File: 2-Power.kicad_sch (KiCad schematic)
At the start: 17 parts, among them J201 DC IN 5.5/2.1mm, J202 9V Battery Connector, U201 ZXMP3A17E6TA

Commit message: Schematic: adding 9V battery clip
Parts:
- J202: LCSC Part # (none) -> -; Mfr (none) -> Keystone; Mfr Part # (none) -> 232; Mouser Part # (none) -> 534-232; Purpose (none) -> connecting the battery to DC IN jack lugs; Source (none) -> Mouser; TME Part # (none) -> KEYS232; now in the parts list
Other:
- note added: "alt: 232-M, 233, 234"
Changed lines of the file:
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@@
+		)
+	)
+	(text "alt: 232-M, 233, 234"
+		(exclude_from_sim no)
+		(at 48.26 83.82 0)
+		(effects
+			(font
+				(size 1 1)
+			)
+			(justify left bottom)
 		)
 	)
@@
 	(text "connected directly to\nDC IN jack lugs"
 		(exclude_from_sim no)
-		(at 48.26 82.55 0)
+		(at 48.26 80.01 0)
 		(effects
 			(font
@@
 		(unit 1)
 		(exclude_from_sim no)
-		(in_bom no)
+		(in_bom yes)
 		(on_board no)
 		(dnp no)
@@
 			)
 		)
-		(property "Datasheet" ""
+		(property "Datasheet" "https://cz.mouser.com/datasheet/2/215/232_234-741236.pdf"
 			(at 39.37 74.295 0)
 			(effects
@@
 			)
 		)
-		(property "Purpose" ""
+		(property "Purpose" "connecting the battery to DC IN jack lugs"
 			(at 39.37 77.47 0)
 			(effects
@@
 					(size 1.27 1.27)
 				)
-			)
-		)
+				(hide yes)
+			)
+		)
+		(property "LCSC Part #" "-"
+			(at 39.37 77.47 0)
+			(effects
+				(font
+					(size 1.27 1.27)
+				)
+				(hide yes)
+			)
+		)
+		(property "Mfr" "Keystone"
+			(at 39.37 77.47 0)
+			(effects
+				(font
+					(size 1.27 1.27)
+				)
+				(hide yes)
+			)
+		)
+		(property "Mfr Part #" "232"
+			(at 39.37 77.47 0)
+			(effects
+				(font
+					(size 1.27 1.27)
+				)
+				(hide yes)
+			)
+		)
+		(property "Mouser Part #" "534-232 "
+			(at 39.37 77.47 0)
+			(effects
+				(font
+					(size 1.27 1.27)
+				)
+				(hide yes)
+			)
+		)
+		(property "Source" "Mouser"
+			(at 39.37 77.47 0)
+			(effects
+				(font
+					(size 1.27 1.27)
+				)
+				(hide yes)
+			)
+		)
+		(property "TME Part #" "KEYS232"
+			(at 39.37 77.47 0)
+			(effects
+				(font
+					(size 1.27 1.27)
+				)
+				(hide yes)
+			)
+		)

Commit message: Schematics: improving Purpose of some components
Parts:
- S201: Purpose ON/OFF switch for DC + true bypass switch for audio -> 4PDT. ON/OFF switch for DC + true bypass switch for audio; Source TME -> Mouser
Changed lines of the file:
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@@
 			)
 		)
-		(property "Purpose" "ON/OFF switch for DC + true bypass switch for audio"
+		(property "Purpose" "4PDT. ON/OFF switch for DC + true bypass switch for audio"
 			(at 49.53 121.92 0)
 			(effects
@@
 			)
 		)
-		(property "Source" "TME"
+		(property "Source" "Mouser"
 			(at 49.53 121.92 0)
 			(effects

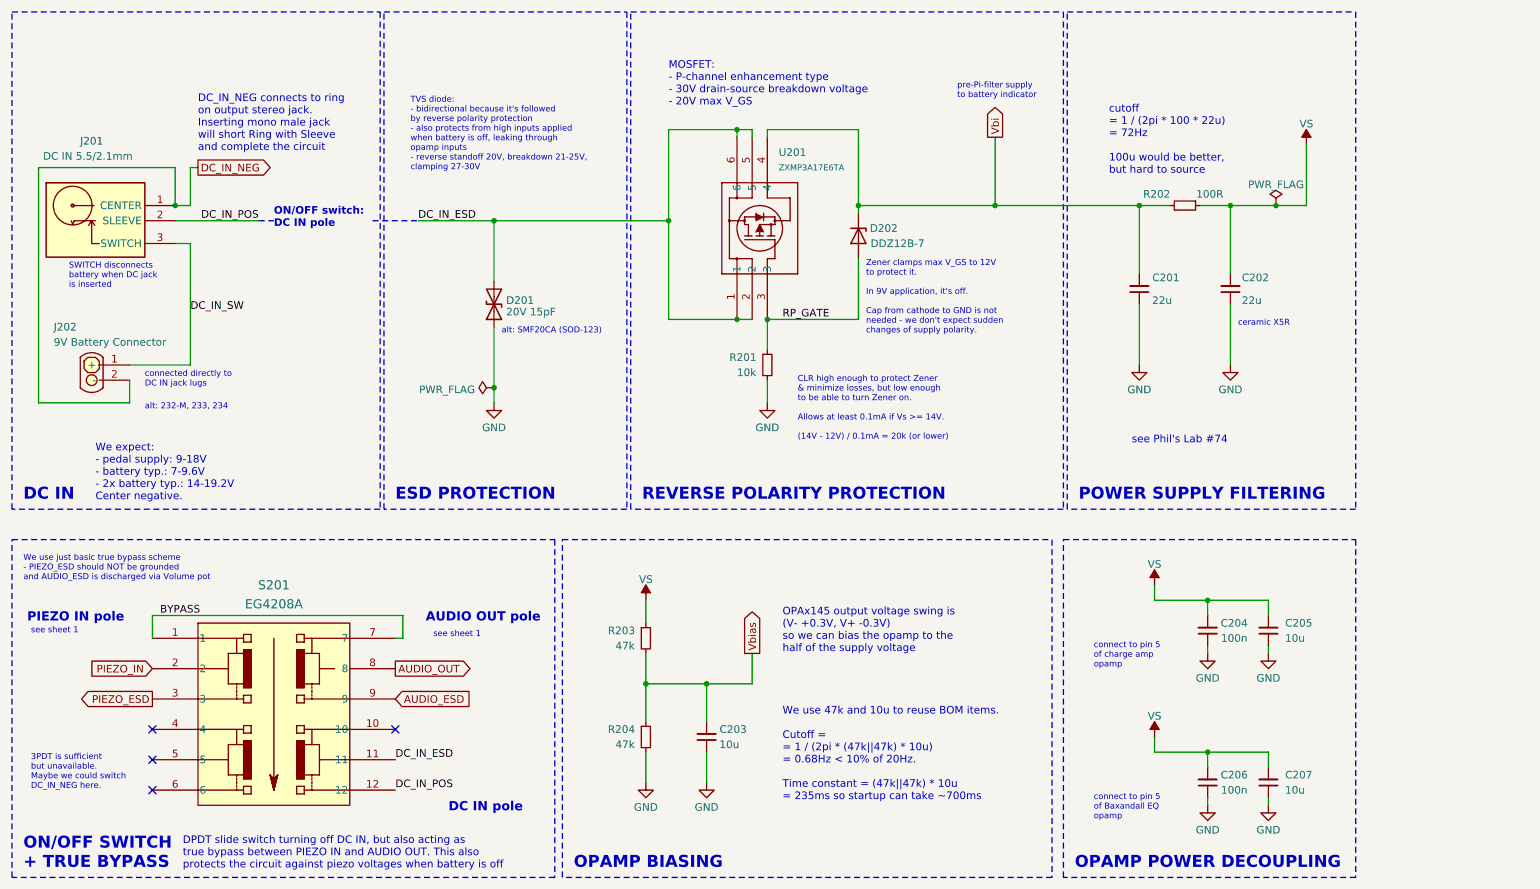
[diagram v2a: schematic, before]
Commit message: Schematic, PCB: moving DC ESD protection in front of the switch. Using one 22uF bulk decoupling cap where DC enters the board instead of two 10uF near opamps. Using 22uF instead of 10uF in opamp biasing to remove 10uF from BOM completely
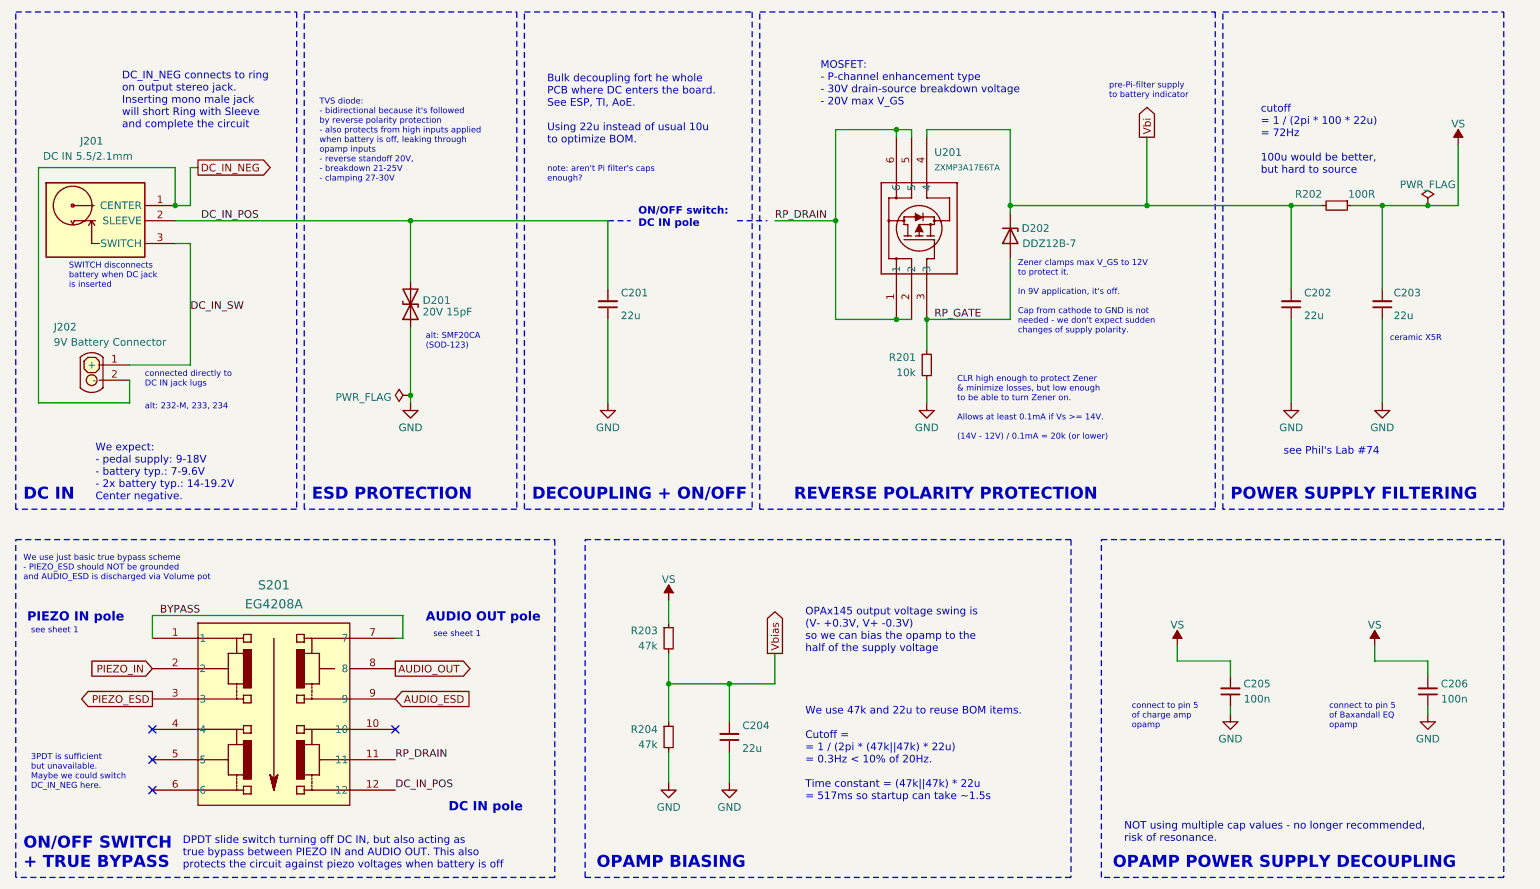
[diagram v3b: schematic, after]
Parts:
- removed C203, C205, C207: 10u, library:cap_CL21A106KAYNNNE, symbol Device:C_Small
- added C201, C204: 22u, library:cap_CL31A226KAHNNNE, symbol Device:C_Small
- renumbered C201 to C202, C202 to C203, C204 to C205
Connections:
- net DC_IN_POS: now also D201.2 (A2), C201.2
- net GND: now also C201.1, C204.1
- net Vbias: now also C204.2
- net DC_IN_ESD renamed RP_DRAIN
- net RP_DRAIN: no longer D201.2 (A2)
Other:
- note added: "Bulk decoupling fort he whole PCB where DC enters the board. See ESP, TI, AoE. Using 22u instead of usual 10u to optimize BOM."
- note added: "DECOUPLING + ON/OFF"
- note added: "NOT using multiple cap values - no longer recommended, risk of resonance."
- note added: "OPAMP POWER SUPPLY DECOUPLING"
- note added: "TVS diode: - bidirectional because it's followed by reverse polarity protection - also protects from high inputs applied when battery is off, leaking through opamp inputs - reverse standoff 20V, - breakdown 21-25V - clamping 27-30V"
- note added: "We use 47k and 22u to reuse BOM items. Cutoff = = 1 / (2pi * (47k||47k) * 22u) = 0.3Hz < 10% of 20Hz. Time constant = (47k||47k) * 22u = 517ms so startup can take ~1.5s"
- note added: "note: aren't Pi filter's caps enough?"
- note removed: "OPAMP POWER DECOUPLING"
- note removed: "TVS diode: - bidirectional because it's followed by reverse polarity protection - also protects from high inputs applied when battery is off, leaking through opamp inputs - reverse standoff 20V, breakdown 21-25V, clamping 27-30V"
- note removed: "We use 47k and 10u to reuse BOM items. Cutoff = = 1 / (2pi * (47k||47k) * 10u) = 0.68Hz < 10% of 20Hz. Time constant = (47k||47k) * 10u = 235ms so startup can take ~700ms"
- moved on the sheet: C202, C203, C205, C206, D201, D202, R201, R202, R203, R204, U201
